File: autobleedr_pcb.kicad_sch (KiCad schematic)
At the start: 17 parts, among them J11 Conn_01x02_Pin, J13 Screw_Terminal_01x08, J2 Conn_01x01_Pin, J7 Screw_Terminal_01x02, U2 ESP32, U6 TMC2209

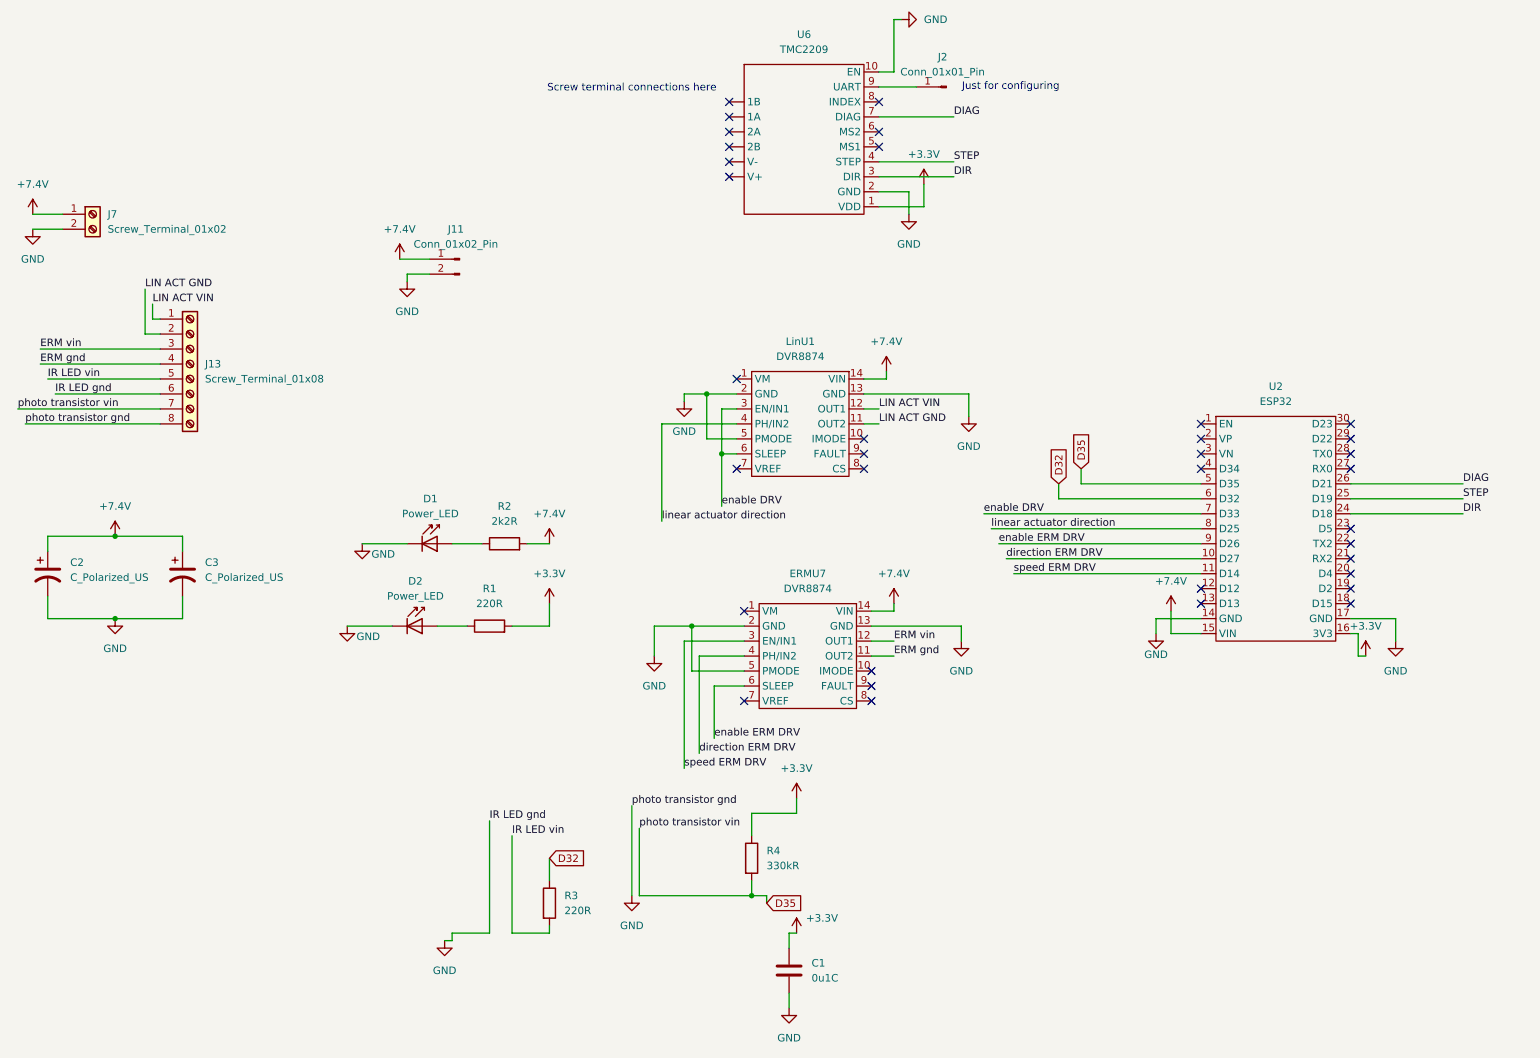
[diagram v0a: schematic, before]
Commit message: updated board with new battery and v2 traces
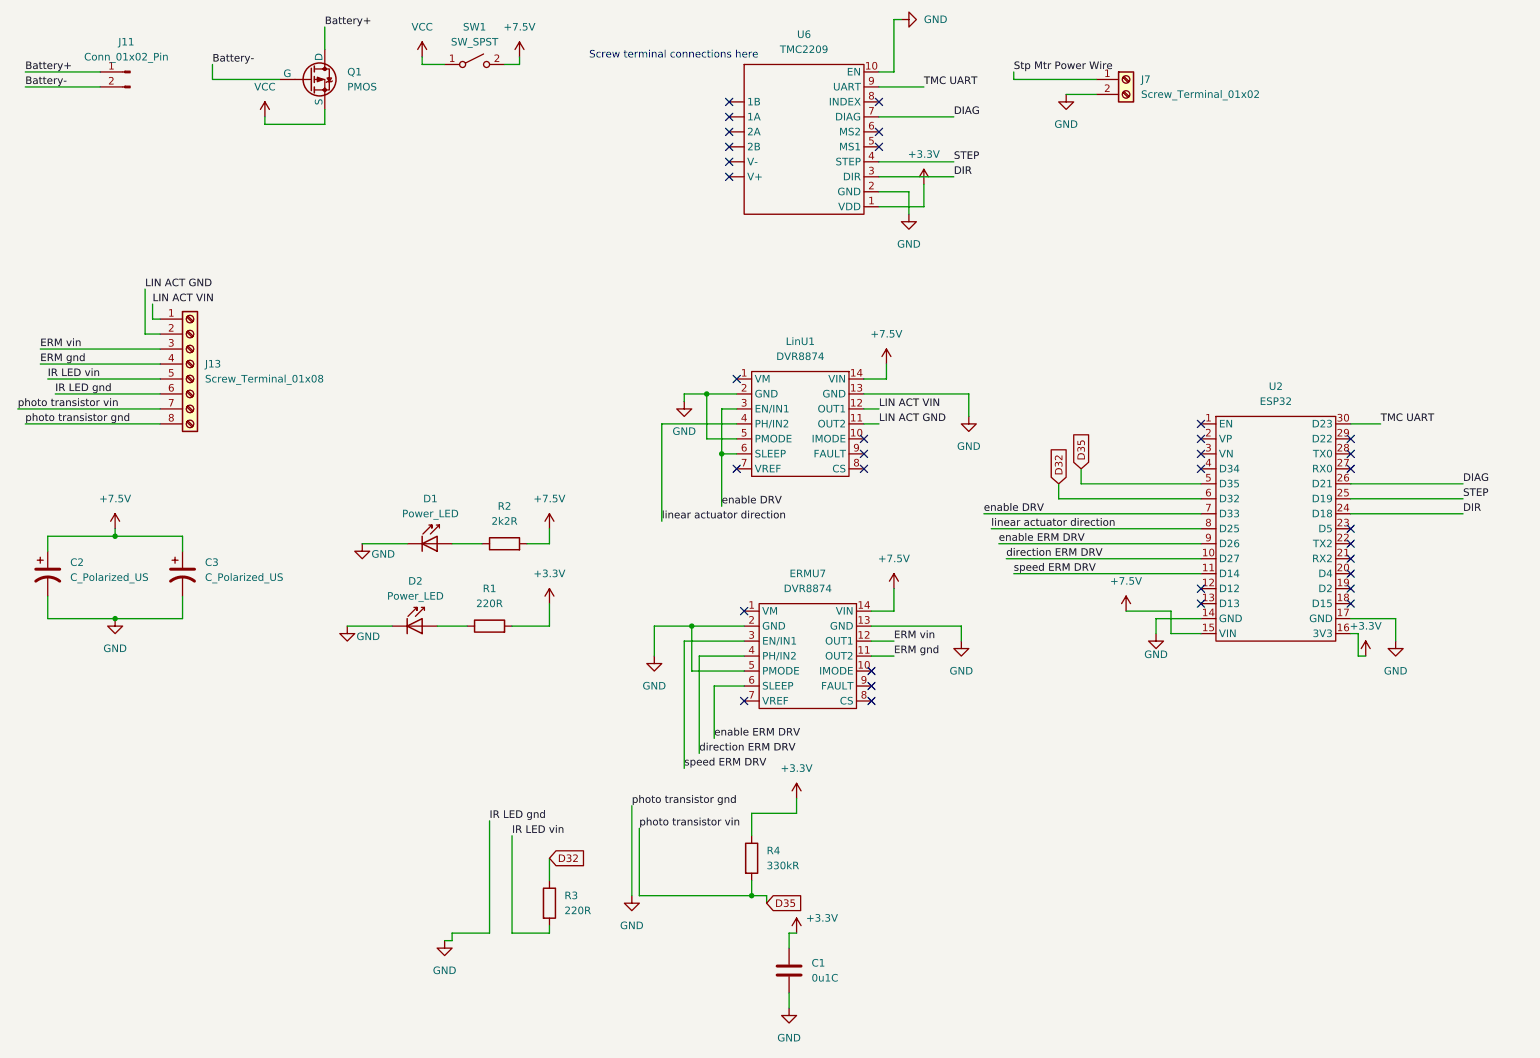
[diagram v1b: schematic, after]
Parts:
- removed J2: Conn_01x01_Pin, Connector_PinHeader_2.54mm:PinHeader_1x01_P2.54mm_Vertical, symbol Connector:Conn_01x01_Pin
- added Q1: PMOS, Capstone_Footprints:DMP6023LE, symbol Simulation_SPICE:PMOS
- added SW1: SW_SPST, Capstone_Footprints:R1966ABLKBLKGR, symbol Switch:SW_SPST
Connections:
- net GND: no longer J11.2 (Pin_2)
- net TMC UART: now reaches U6.9 (UART)
- net TMC UART: now also U2.30 (D23)
- net +7.4V renamed +7.5V
- net +7.5V: now also SW1.2 (B); no longer J11.1 (Pin_1), J7.1 (Pin_1)
- new net Battery+: J11.1 (Pin_1), Q1.4 (D)
- new net Battery-: J11.2 (Pin_2), Q1.1 (G)
- new net Stp Mtr Power Wire: J7.1 (Pin_1)
- new net VCC: Q1.3 (S), SW1.1 (A)
- no-connect marks 35 -> 34
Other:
- note removed: "Just for configuring"
- moved on the sheet: J11, J7

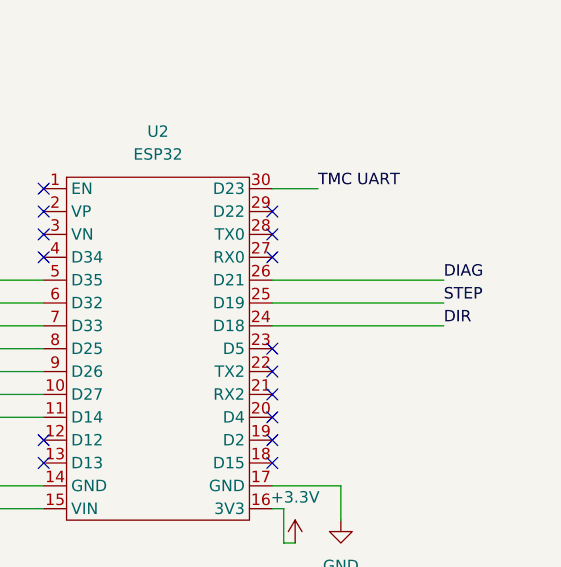
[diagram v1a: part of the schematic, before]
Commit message: Added uart connection
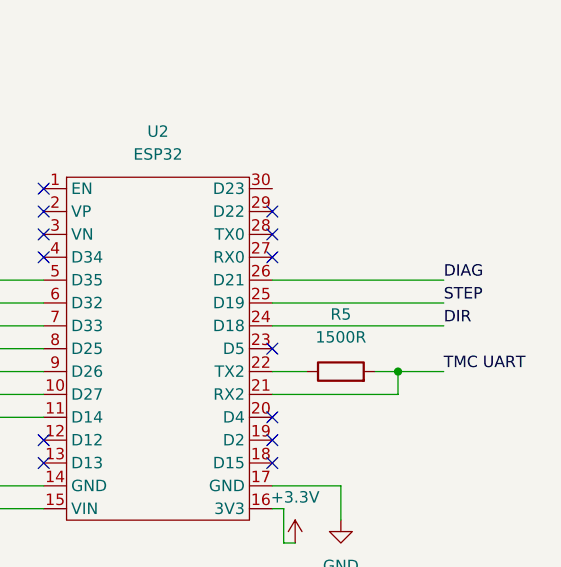
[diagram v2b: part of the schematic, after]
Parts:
- added R5: 1500R, Resistor_THT:R_Axial_DIN0207_L6.3mm_D2.5mm_P7.62mm_Horizontal, symbol Device:R
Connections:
- net TMC UART: now also U2.21 (RX2), R5.2; no longer U2.30 (D23)
- net at U2.22 (TX2): now also R5.1
- no-connect marks 34 -> 32
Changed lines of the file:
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@@
 		(color 0 0 0 0)
 	)
+	(junction
+		(at 257.81 107.95)
+		(diameter 0)
+		(color 0 0 0 0)
+	)
 	(no_connect
 		(at 163.83 40.64)
@@
 	)
 	(no_connect
-		(at 243.84 110.49)
-	)
-	(no_connect
-		(at 243.84 107.95)
-	)
-	(no_connect
 		(at 243.84 95.25)
 	)
@@
 	(wire
 		(pts
+			(xy 257.81 110.49) (xy 257.81 107.95)
+		)
+		(stroke
+			(width 0)
+			(type default)
+		)
+	)
+	(wire
+		(pts
 			(xy 140.97 129.54) (xy 132.08 129.54)
 		)
@@
 	(wire
 		(pts
+			(xy 243.84 110.49) (xy 257.81 110.49)
+		)
+		(stroke
+			(width 0)
+			(type default)
+		)
+	)
+	(wire
+		(pts
 			(xy 91.44 175.26) (xy 91.44 173.99)
 		)
@@
 	(wire
 		(pts
-			(xy 243.84 87.63) (xy 248.92 87.63)
-		)
-		(stroke
-			(width 0)
-			(type default)
-		)
-	)
-	(wire
-		(pts
 			(xy 45.72 116.84) (xy 45.72 120.65)
 		)
@@
 	(wire
 		(pts
+			(xy 243.84 107.95) (xy 247.65 107.95)
+		)
+		(stroke
+			(width 0)
+			(type default)
+		)
+	)
+	(wire
+		(pts
 			(xy 101.6 173.99) (xy 107.95 173.99)
 		)
@@
 	(wire
 		(pts
+			(xy 257.81 107.95) (xy 262.89 107.95)
+		)
+		(stroke
+			(width 0)
+			(type default)
+		)
+	)
+	(wire
+		(pts
 			(xy 86.36 26.67) (xy 86.36 25.4)
 		)
@@
 		(pts
 			(xy 139.7 87.63) (xy 127 87.63)
+		)
+		(stroke
+			(width 0)
+			(type default)
+		)
+	)
+	(wire
+		(pts
+			(xy 255.27 107.95) (xy 257.81 107.95)
 		)
 		(stroke
@@
 		)
 	)
+	(label "TMC UART"
+		(at 262.89 107.95 0)
+		(effects
+			(font
+				(size 1.27 1.27)
+			)
+			(justify left bottom)
+		)
+	)
 	(label "direction ERM DRV"
 		(at 185.42 110.49 0)
@@
 	(label "Battery-"
 		(at 50.8 26.67 0)
-		(effects
-			(font
-				(size 1.27 1.27)
-			)
-			(justify left bottom)
-		)
-	)
-	(label "TMC UART"
-		(at 248.92 87.63 0)
 		(effects
 			(font
@@
 					(unit 1)
 				)
+			)
+		)
+	)
+	(symbol
+		(lib_id "Device:R")
+		(at 251.46 107.95 90)
+		(unit 1)
+		(exclude_from_sim no)
+		(in_bom yes)
+		(on_board yes)
+		(dnp no)
+		(fields_autoplaced yes)
+		(property "Reference" "R5"
+			(at 251.46 101.6 90)
+			(effects
+				(font
+					(size 1.27 1.27)
+				)
+			)
+		)
+		(property "Value" "1500R"
+			(at 251.46 104.14 90)
+			(effects
+				(font
+					(size 1.27 1.27)
+				)
+			)
+		)
+		(property "Footprint" "Resistor_THT:R_Axial_DIN0207_L6.3mm_D2.5mm_P7.62mm_Horizontal"
+			(at 251.46 109.728 90)
+			(effects
+				(font
+					(size 1.27 1.27)
+				)
+				(hide yes)
+			)
+		)
+		(property "Datasheet" "~"
+			(at 251.46 107.95 0)
+			(effects
+				(font
+					(size 1.27 1.27)
+				)
+				(hide yes)
+			)
+		)
+		(property "Description" "Resistor"
+			(at 251.46 107.95 0)
+			(effects
+				(font
+					(size 1.27 1.27)
+				)
+				(hide yes)
+			)
+		)
+		(pin "2"
+		)
+		(pin "1"
+		)
+		(instances
+			(project "autobleedr_pcb"
+				(path "/1cb070e6-4268-4590-be3a-70f1be021dfd"
+					(reference "R5")
+					(unit 1)
+				)

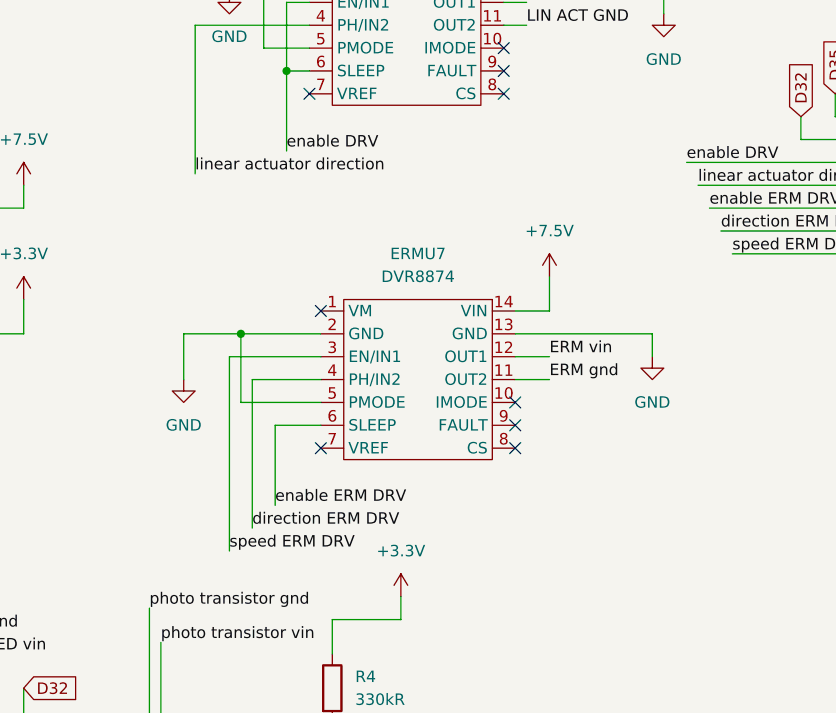
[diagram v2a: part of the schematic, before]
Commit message: Added UART Resistor and the modified ERM driver.
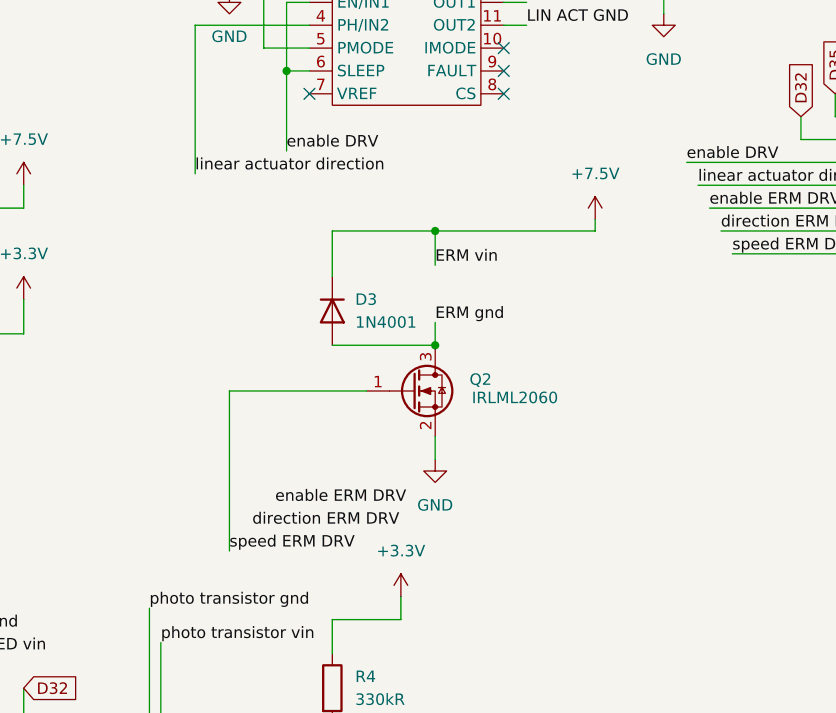
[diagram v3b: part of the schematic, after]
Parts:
- removed ERMU7: DVR8874, Capstone_Footprints:DVR8874, symbol Capstone_Symbols:DVR8874
- added D3: 1N4001, Diode_THT:D_DO-41_SOD81_P10.16mm_Horizontal, symbol Diode:1N4001
- added Q2: IRLML2060, Package_TO_SOT_SMD:SOT-23, symbol Transistor_FET:IRLML2060
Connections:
- net ERM vin is gone; now on net +7.5V: J13.3 (Pin_3)
- net +7.5V: now also D3.1 (K)
- net ERM gnd: now also D3.2 (A), Q2.3 (D)
- net GND: now also Q2.2 (S)
- net speed ERM DRV: now also Q2.1 (G)
- no-connect marks 32 -> 27
